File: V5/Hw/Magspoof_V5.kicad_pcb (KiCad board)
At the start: 2 copper layers, 76.5 x 32.5 mm, 50 parts, among them J2 SWD, P1 USB_C_Plug_USB2.0, Q1 DMG3415U-7, SW1 ON, SW3 S1, SW4 SOURCE MAG, SW5 RESET, U1 CH552G, U2 AP2112K-3.3, U3 TC4424, U5 MCP73831

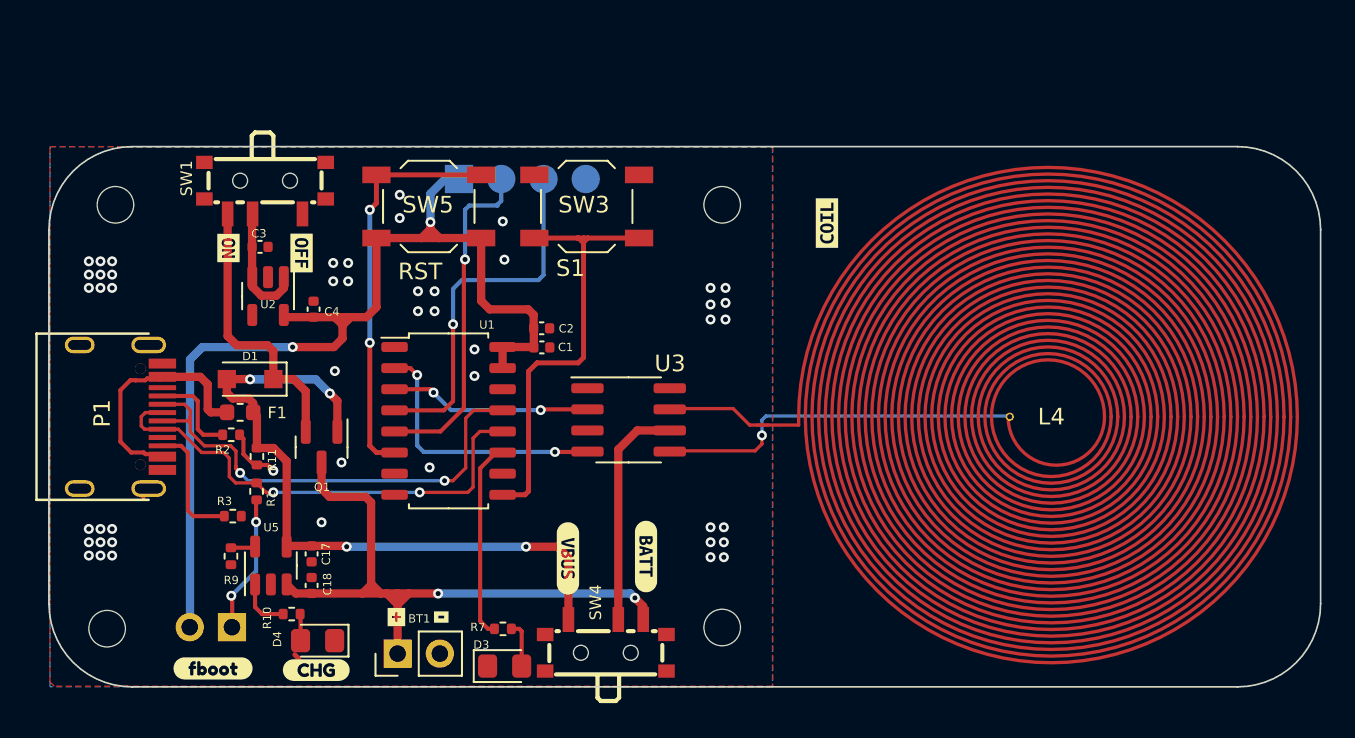
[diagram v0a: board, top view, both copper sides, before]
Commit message: feat(hw): components got reorganized
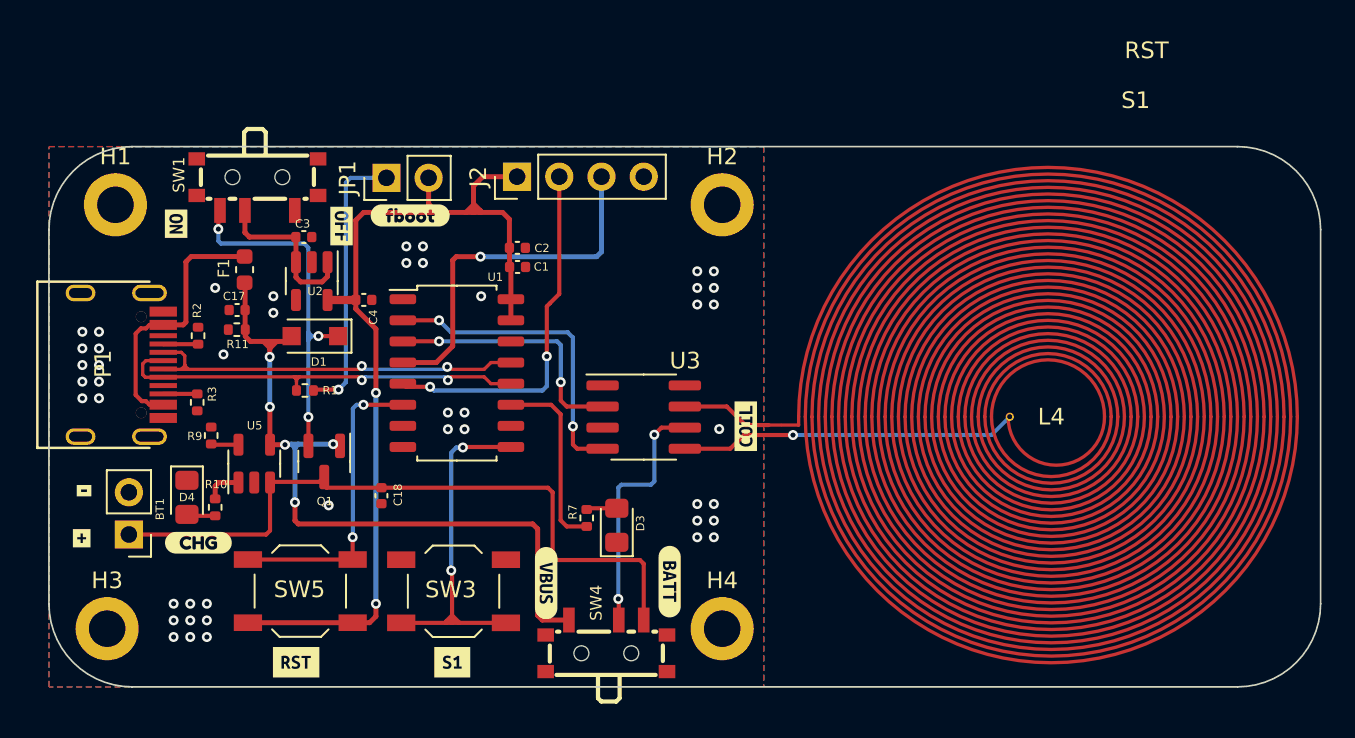
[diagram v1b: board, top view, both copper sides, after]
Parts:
- added kibuzzard-660F1CC0: G***, kibuzzard-660F1CC0, F.Cu at (113.4, 64.5)
- added kibuzzard-660F1CCE: G***, kibuzzard-660F1CCE, F.Cu at (122.8, 64.5)
- H1, H2, H3, H4: footprint MountingHole:MountingHole_2.2mm_M2 -> MountingHole:MountingHole_2.2mm_M2_DIN965_Pad
- J2, JP1: moved to F.Cu
- moved kibuzzard-64665C9F 29.7 mm to (120.2, 37.6)
- moved JP1 28.6 mm to (118.8, 35.4)
- moved SW3 24.5 mm to (122.8, 60.2)
- moved SW5 24.4 mm to (113.6, 60.2)
- moved kibuzzard-6436EA46 22.8 mm to (100.6, 54.2)
- moved kibuzzard-6436EA37 19.5 mm to (100.5, 57.1)
- moved BT1 17.7 mm to (103.3, 56.8), turned to 180 degrees
- moved C17 15.3 mm to (109.8, 43.3), turned to 180 degrees
- moved kibuzzard-6435F3C4 13.2 mm to (140.4, 50.3)
- moved REF** 12.7 mm to (129.4, 55.0)
- moved D4 11.7 mm to (106.8, 54.6), turned to -90 degrees
- moved D3 10.8 mm to (132.7, 56.3), turned to 90 degrees
- moved kibuzzard-64665C6A 10.4 mm to (107.5, 57.3)
- moved F1 8.59 mm to (110.3, 40.9), turned to -90 degrees
- moved R7 8.36 mm to (130.8, 55.8), turned to 90 degrees
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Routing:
- net Net-(JP1-A): track 8.32 -> 16.7 mm, vias 2 -> 1
- net /RST: track 24.4 -> 18.5 mm
- net Net-(P1-VCONN): track 7.52 -> 2.05 mm
- net /SW1: track 26.9 -> 21.5 mm, vias 0 -> 2
- net /D-: track 29.3 -> 24.3 mm
- net Net-(D1-K): track 16.8 -> 21.8 mm, vias 0 -> 3
- net +3V3: track 62.9 -> 59.0 mm
- net GND: track 3.77 -> 0.00 mm, vias 49 -> 46
- net Net-(P1-CC): track 5.59 -> 2.10 mm
- net /IN_B: track 12.1 -> 15.6 mm
- net /D+: track 29.2 -> 26.1 mm
- net /IN_A: track 16.2 -> 19.0 mm
- net Net-(SW1-B): track 7.36 -> 9.94 mm
- net +BATT: track 39.6 -> 42.2 mm, vias 2 -> 0
- net VBUS: track 42.8 -> 44.9 mm, vias 4 -> 5
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
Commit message: feat(hw): TX and RX pins updated
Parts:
- moved kibuzzard-6436EF98 0.58 mm to (115.5, 38.2)
- moved kibuzzard-6436EF9F 0.43 mm to (106.5, 38.0)
- moved kibuzzard-6436EA46 0.28 mm to (100.3, 54.1)
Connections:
- U1 pad 4: /RXD -> unconnected-(U1-P1.6-Pad4)
- U1 pad 5: /TXD -> unconnected-(U1-P1.7-Pad5)
- U1 pad 7: unconnected-(U1-P3.1-Pad7) -> /TXD
- U1 pad 8: unconnected-(U1-P3.0-Pad8) -> /RXD
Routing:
- net /RXD: track 22.3 -> 27.6 mm
- net /TXD: track 21.9 -> 23.8 mm
- net GND: vias 46 -> 48
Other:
- board text removed: "RST"
- board text removed: "S1"

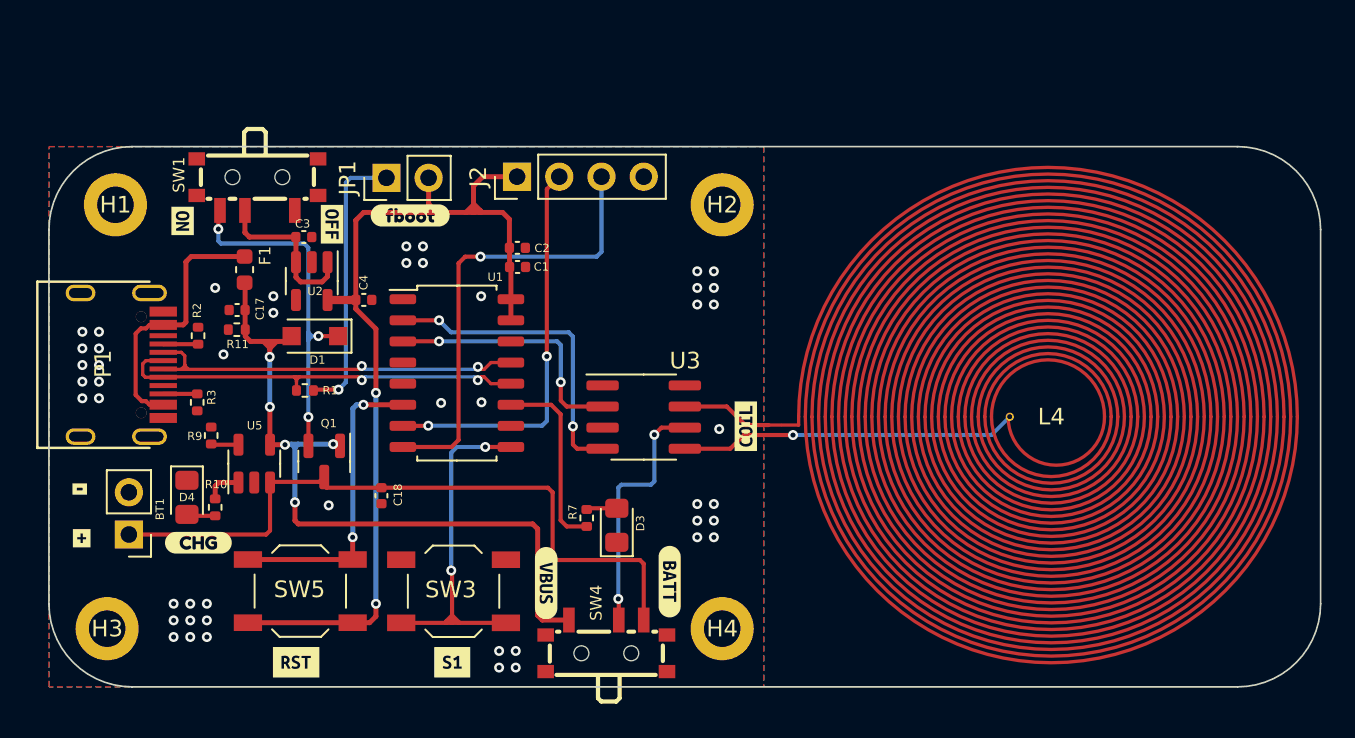
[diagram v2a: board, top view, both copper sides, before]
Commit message: feat(hw): path width changed
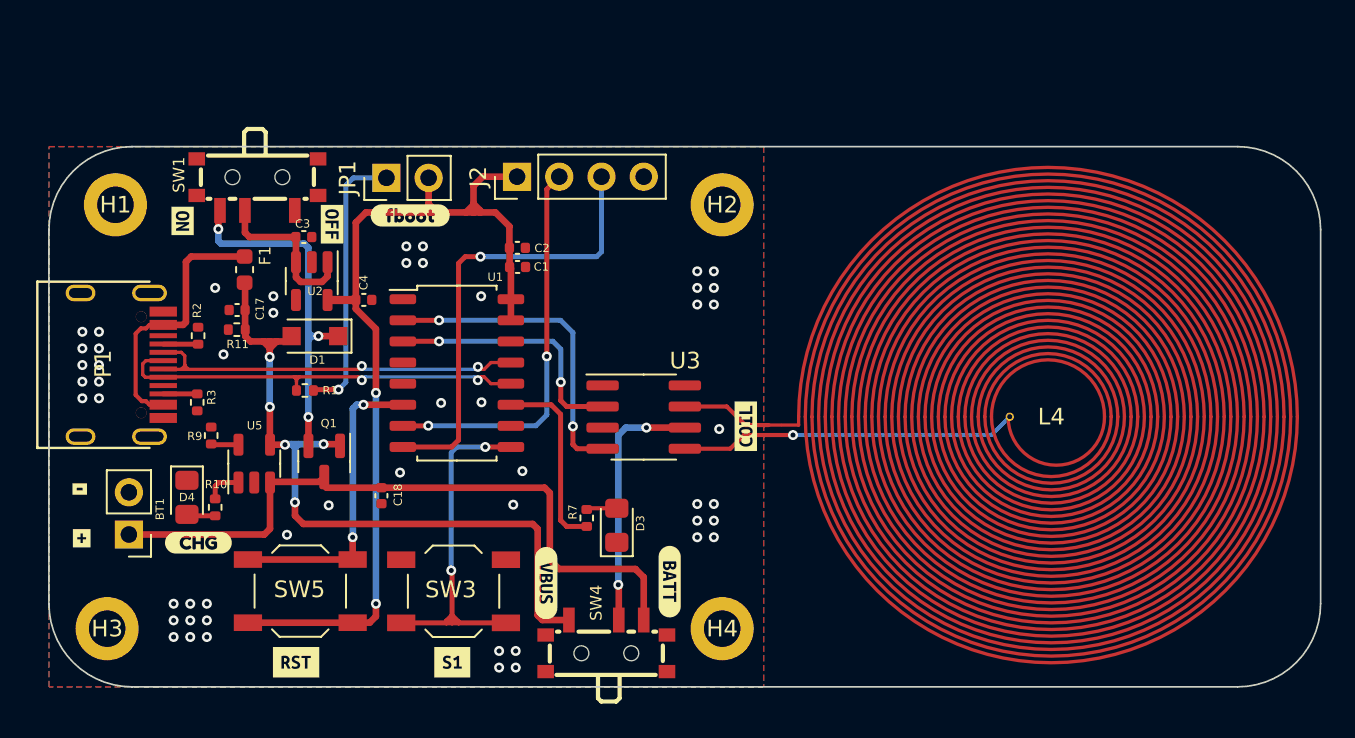
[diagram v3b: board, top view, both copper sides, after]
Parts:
- moved G*** 1.07 mm to (129.8, 44.8)
- moved REF** 0.87 mm to (129.8, 54.1)
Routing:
- net GND: vias 48 -> 52

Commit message: fix(hw): Some paths got corrections
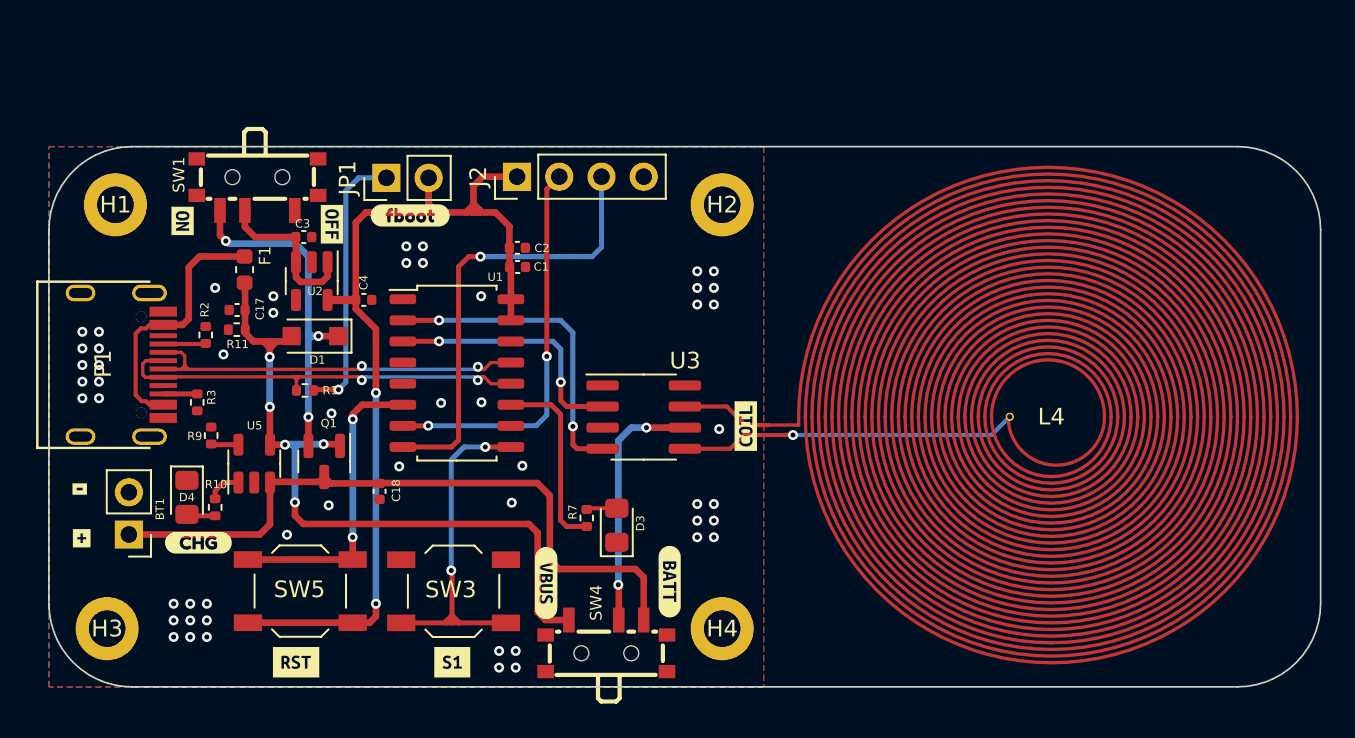
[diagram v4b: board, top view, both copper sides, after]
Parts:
- moved R2 0.46 mm to (107.9, 44.8)
- moved C18 0.28 mm to (118.4, 54.2)
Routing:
- net Net-(D1-K): track 21.8 -> 21.2 mm
- net +BATT: track 41.8 -> 41.2 mm
- net GND: vias 52 -> 53

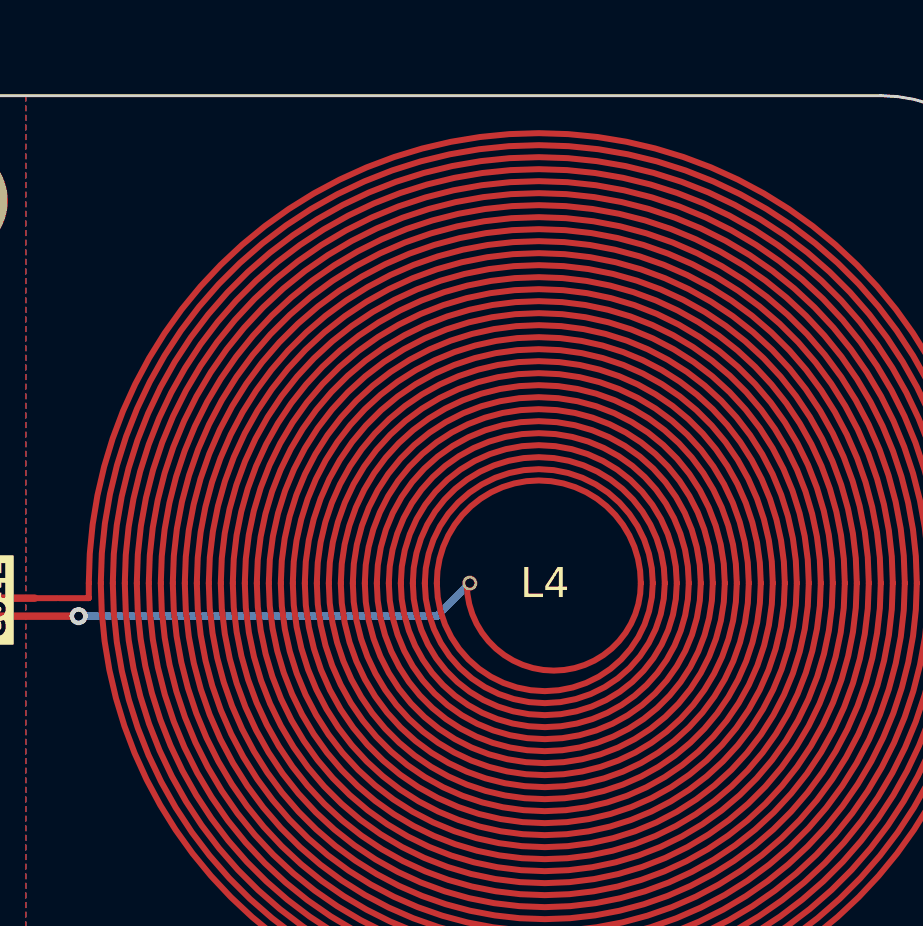
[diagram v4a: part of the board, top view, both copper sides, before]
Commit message: feat(hw): add logos
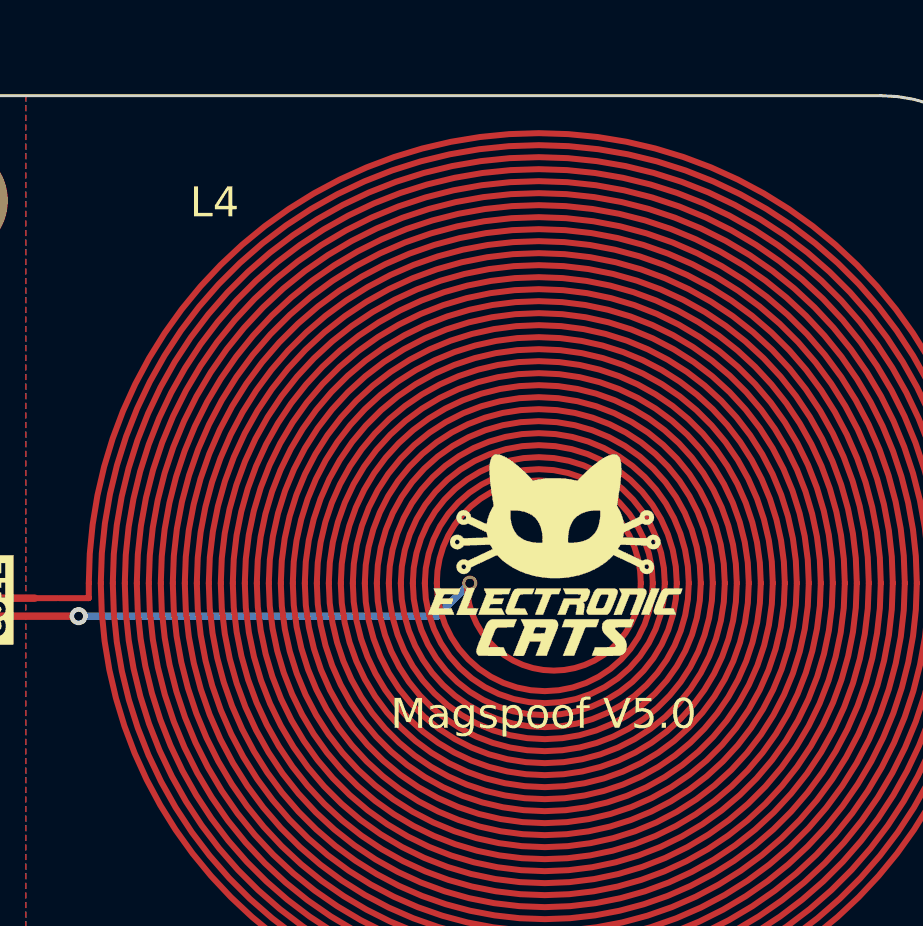
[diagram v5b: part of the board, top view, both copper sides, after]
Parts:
- added G***: LOGO, Aesthetics:electronic_cats_logo_8x6, F.Cu at (159.2, 48.8)
- moved REF** 29.6 mm to (158.8, 48.0)
- moved G*** 5.69 mm to (124.9, 47.7)

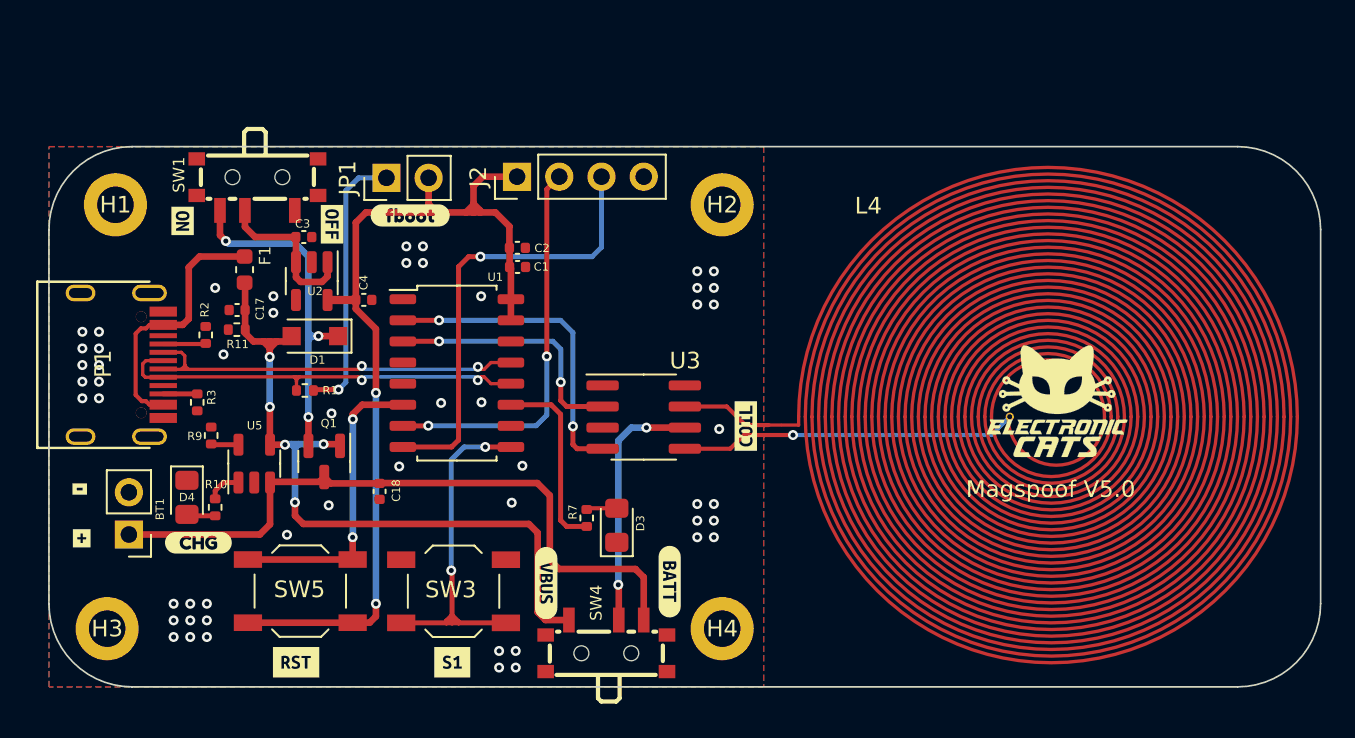
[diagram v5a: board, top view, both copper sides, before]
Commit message: feat(hw): added TX and RX Boot pins
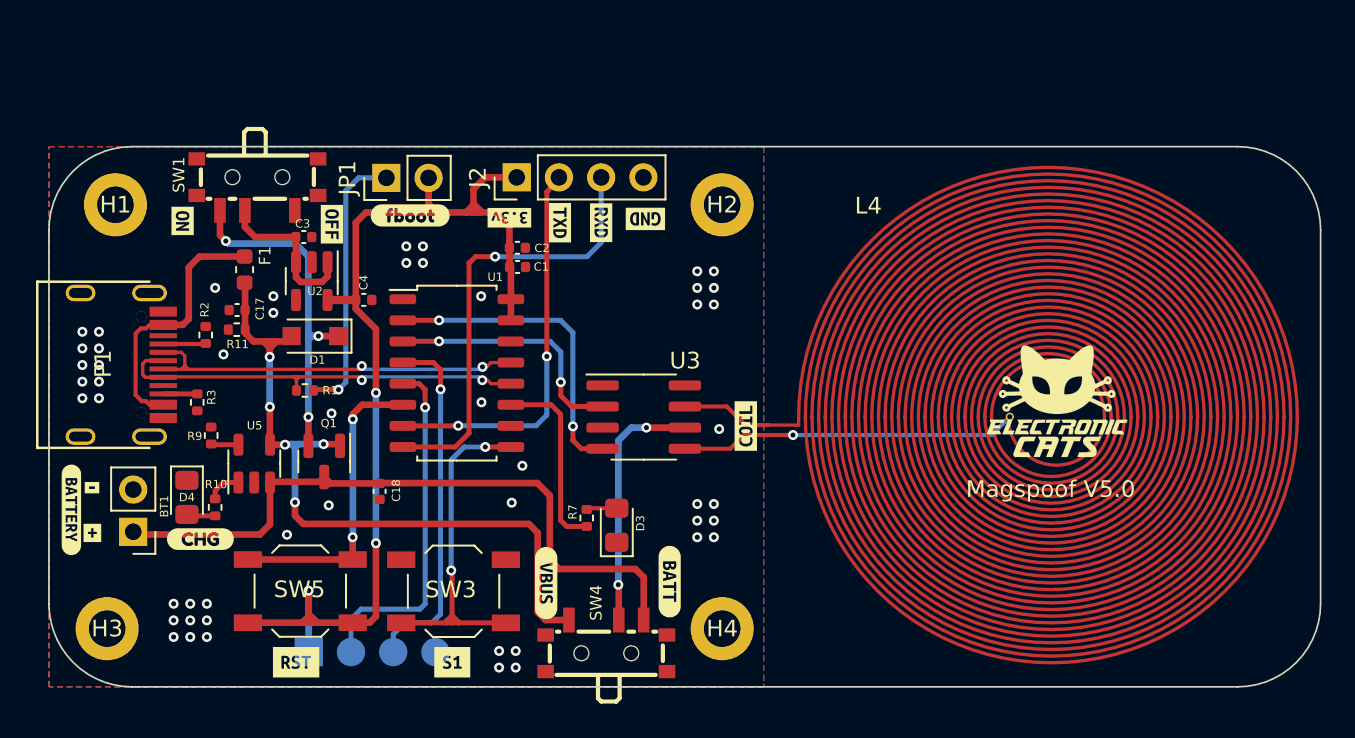
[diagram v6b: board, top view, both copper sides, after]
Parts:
- removed kibuzzard-6435F22E: G***, kibuzzard-6435F22E
- added J2: SWD, Connector_PinHeader_2.54mm:PinHeader_1x04_P2.54mm_Vertical, F.Cu at (126.6, 35.4)
- added kibuzzard-6616D983: G***, kibuzzard-6616D983, B.Cu at (113.1, 60.6)
- added kibuzzard-6616D9B1: G***, kibuzzard-6616D9B1, B.Cu at (116.4, 60.2)
- added kibuzzard-6616D9C5: G***, kibuzzard-6616D9C5, B.Cu at (119.4, 60.3)
- added kibuzzard-6616D9E2: G***, kibuzzard-6616D9E2, B.Cu at (122.1, 60.7)
- added kibuzzard-6616DB9C: G***, kibuzzard-6616DB9C, F.Cu at (126.2, 37.8)
- added kibuzzard-6616DCE6: G***, kibuzzard-6616DCE6, F.Cu at (99.8, 55.4)
- J1: renamed from J2; moved to B.Cu
- kibuzzard-6435F1C7, kibuzzard-6436E8D1, kibuzzard-6436E8D8: moved to F.Cu
- moved J1 31.2 mm to (114.1, 63.9), turned to -90 degrees
- moved kibuzzard-6436EA46 0.74 mm to (101.1, 54.0)
- moved kibuzzard-6436EA37 0.72 mm to (101.1, 56.7)
- moved BT1 0.31 mm to (103.6, 56.7)
- moved kibuzzard-64665C6A 0.25 mm to (107.6, 57.1)
- moved kibuzzard-6435F1C7 0.23 mm to (134.4, 37.9), turned to 180 degrees
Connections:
- J1 pad 2: /TXD -> /TXD_BOOT
- J1 pad 3: /RXD -> /RXD_BOOT
- U1 pad 4: unconnected-(U1-P1.6-Pad4) -> /RXD_BOOT
- U1 pad 5: unconnected-(U1-P1.7-Pad5) -> /TXD_BOOT
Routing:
- net /RXD_BOOT: track 0.00 -> 21.6 mm, vias 0 -> 1
- net /TXD_BOOT: track 0.00 -> 21.2 mm, vias 0 -> 1
- net +3V3: track 58.7 -> 65.8 mm, vias 2 -> 3
- net GND: vias 53 -> 51
